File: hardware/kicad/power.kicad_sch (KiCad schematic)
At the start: 61 parts, among them J1 USB_C_Receptacle_USB2.0_16P, J2 BATT (1S LiPo), U1 BQ24073RGT, U2 TPS63802DLA, U3 TPS61023DRL, U4 TPS22965DSG, U5 USBLC6-2SC6, U6 TPS63900DSK, U7 MCP1700T-3002E/TT

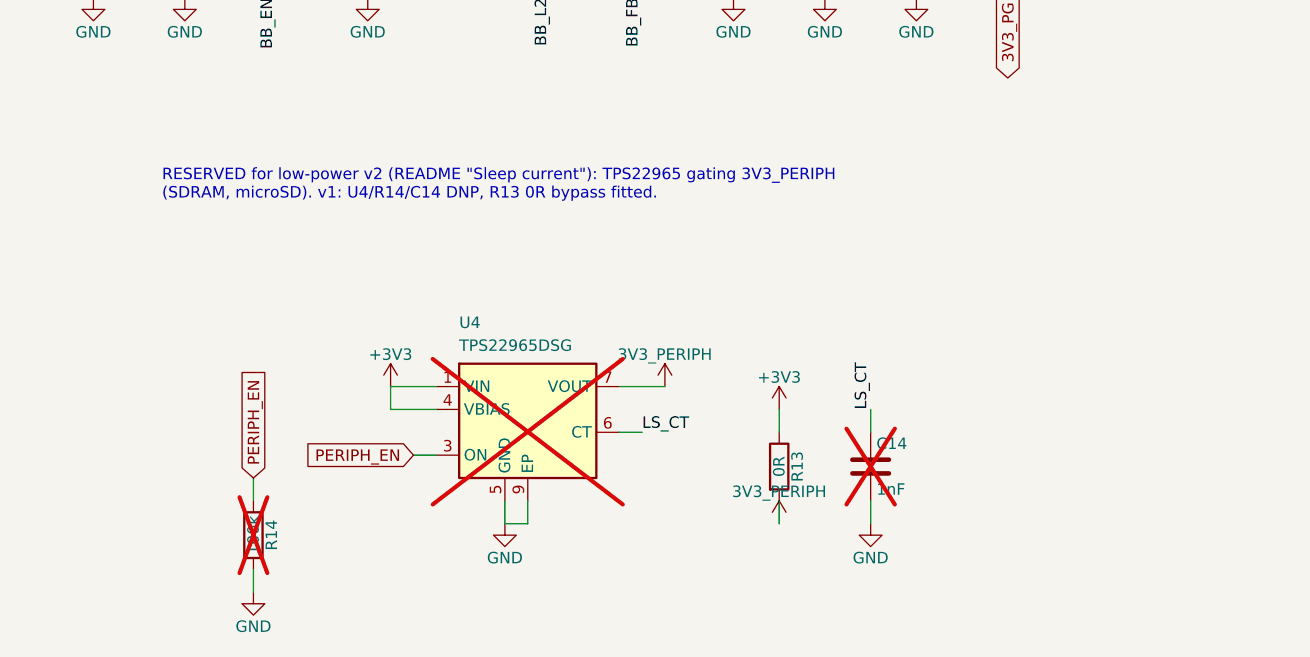
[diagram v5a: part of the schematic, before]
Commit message: Fit the TPS22965 peripheral load switch on v1
Without it SDRAM/QSPI/microSD stay powered in STANDBY (~2-20 mA idle floor,
~70 mAh/day); with it idle drops to ~0.5-2 mAh/day.

- U4 TPS22965 populated; R13 0R bypass -> DNP (fallback).
- R14 100k pull-down on PERIPH_EN (PD7) fitted: rail off at reset and
  automatically in STANDBY (GPIO hi-Z).
- C14 CT 1 nF, 25 V X7R (CT pin reaches 12 V): ~1.3 ms rise at 3.3 V
  (datasheet Table 1) -> ~50 mA inrush into ~21 uF of downstream decoupling.
- README/TODO: decision, firmware sequencing rules (enable before
  FMC/QSPI/SDIO init; pins to analog/low before disabling; re-init SDRAM and
  re-mount SD on wake), TPS63900 remains the only v2 reservation.

ERC 0 violations; check_schematic.py OK.

Co-Authored-By: Claude Opus 5.5 <noreply@anthropic.com>
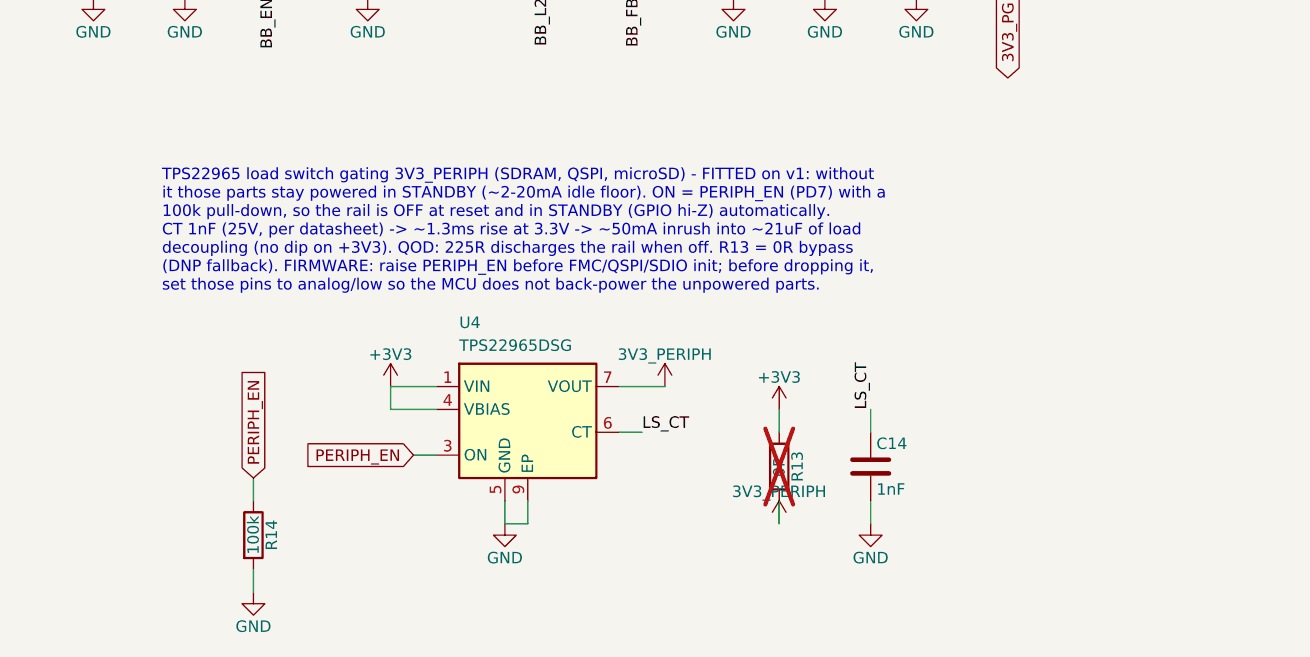
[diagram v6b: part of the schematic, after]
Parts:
- C14: Voltage (none) -> 25V X7R (CT pin can reach 12V); now fitted
- R13: now not fitted
- R14, U4: now fitted
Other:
- note added: "TPS22965 load switch gating 3V3_PERIPH (SDRAM, QSPI, microSD) - FITTED on v1: without it those parts stay powered in STANDBY (~2-20mA idle floor). ON = PERIPH_EN (PD7) with a 100k pull-down, so the rail is OFF at reset and in STANDBY (GPIO hi-Z) automatically. CT 1nF (25V, per datasheet) -> ~1.3ms rise at 3.3V -> ~50mA inrush into ~21uF of load decoupling (no dip on +3V3). QOD: 225R discharges th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"
- note removed: "RESERVED for low-power v2 (README "Sleep current"): TPS22965 gating 3V3_PERIPH (SDRAM, microSD). v1: U4/R14/C14 DNP, R13 0R bypass fitted."
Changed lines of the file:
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@@
 		)
 	)
-	(text "RESERVED for low-power v2 (README \"Sleep current\"): TPS22965 gating 3V3_PERIPH\n(SDRAM, microSD). v1: U4/R14/C14 DNP, R13 0R bypass fitted."
+	(text "TPS22965 load switch gating 3V3_PERIPH (SDRAM, QSPI, microSD) - FITTED on v1: without\nit those parts stay powered in STANDBY (~2-20mA idle floor). ON = PERIPH_EN (PD7) with a\n100k pull-down, so the rail is OFF at reset and in STANDBY (GPIO hi-Z) automatically.\nCT 1nF (25V, per datasheet) -> ~1.3ms rise at 3.3V -> ~50mA inrush into ~21uF of load\ndecoupling (no dip on +3V3). QOD: 225R discharges the rail when off. R13 = 0R bypass\n(DNP fallback). FIRMWARE: raise PERIPH_EN before FMC/QSPI/SDIO init; before dropping it,\nset those pins to analog/low so the MCU does not back-power the unpowered parts."
 		(exclude_from_sim no)
 		(at 137.16 236.22 0)
@@
 		(in_bom yes)
 		(on_board yes)
-		(dnp yes)
+		(dnp no)
 		(property "Reference" "U4"
 			(at 170.18 254 0)
@@
 		(in_bom yes)
 		(on_board yes)
-		(dnp no)
+		(dnp yes)
 		(property "Reference" "R13"
 			(at 207.772 269.24 90)
@@
 		(in_bom yes)
 		(on_board yes)
-		(dnp yes)
+		(dnp no)
 		(property "Reference" "R14"
 			(at 149.352 276.86 90)
@@
 		(in_bom yes)
 		(on_board yes)
-		(dnp yes)
+		(dnp no)
 		(property "Reference" "C14"
 			(at 216.535 266.7 0)
@@
 			(at 215.9 269.24 0)
 			(hide yes)
+			(effects
+				(font
+					(size 1.27 1.27)
+				)
+			)
+		)
+		(property "Voltage" "25V X7R (CT pin can reach 12V)"
+			(at 215.9 269.24 0)
+			(hide yes)

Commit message: Apply enclosure decisions: bottom-edge power button, electrode boards, leaded NTC
Decisions (2026-09-23): keep the HAT's 2x20 header for v1; move the power
button to the bottom edge; put the side-wall electrodes on two small
boards; keep the front-face knob; put RT1 on leads to the cell.

Schematic (via the generator scripts, check_schematic.py passes):
- SW302: Alps SKRTLAE010 side-actuated switch on the PCB's bottom edge.
- E301-E304 test pads -> J302/J303 JST-SH 3-pin (touch / GND / touch),
  cabled to the electrode boards.
- RT1: leaded Murata NXFT15XH103FA2B (same 10k/B3380 curve) on solder
  pads, head taped to the pouch.

Enclosure: flexure tab in the bottom wall over the switch; two identical
74 x 10 mm electrode boards in printed channels on the side walls; PCB
and battery 2.5 mm in from the walls to make room; new checks for the
button travel and electrode coverage (21 pass, no interferences);
electrode_board.json export and a bottom-edge render.

Co-Authored-By: Claude Opus 5.5 <noreply@anthropic.com>
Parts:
- RT1: footprint Resistor_SMD:R_0402_1005Metric -> Connector_Wire:SolderWire-0.1sqmm_1x02_P3.6mm_D0.4mm_OD1mm; MPN NCP15XH103F03RC (10k, B=3380; TS thresholds assume 103AT, B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 -> NXFT15XH103FA2B (Murata leaded film NTC: same 10k/B=3380 cu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
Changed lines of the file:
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@@
 			)
 		)
-		(property "Footprint" "Resistor_SMD:R_0402_1005Metric"
+		(property "Footprint" "Connector_Wire:SolderWire-0.1sqmm_1x02_P3.6mm_D0.4mm_OD1mm"
 			(at 172.72 111.76 0)
 			(hide yes)
@@
 			)
 		)
-		(property "MPN" "NCP15XH103F03RC (10k, B=3380; TS thresholds assume 103AT, B=3435) - place touching the cell"
+		(property "MPN" "NXFT15XH103FA2B (Murata leaded film NTC: same 10k/B=3380 curve as NCP15XH103; TS thresholds assume 103AT, B=3435) - leads soldered here, head taped to the cell (it sits beside the PCB)"
 			(at 172.72 111.76 0)
 			(hide yes)

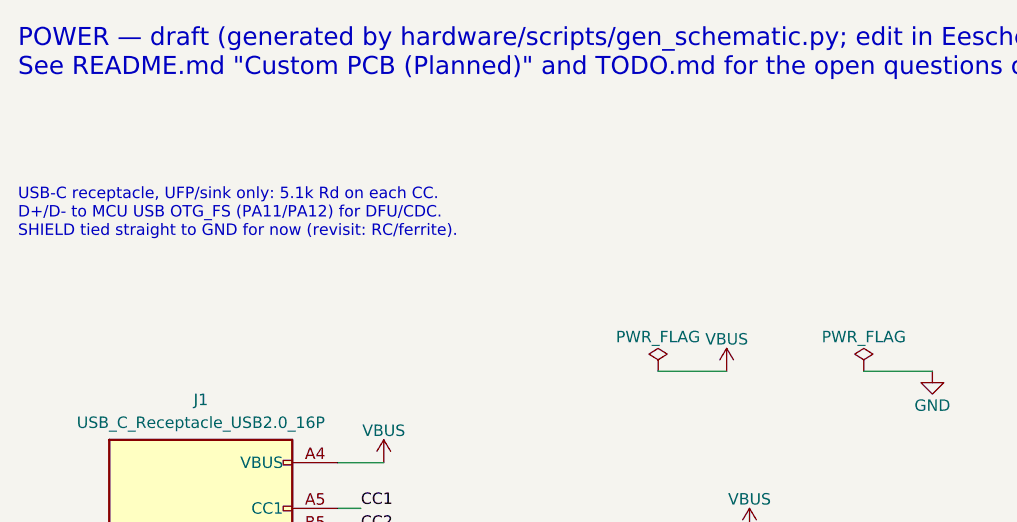
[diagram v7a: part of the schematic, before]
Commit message: Electrode board project, open hardware TODOs, main PCB bootstrap
- hardware/electrode/: side-wall electrode board (one design, two fitted),
  generated by gen_electrode.py (schematic, pad footprint) and
  gen_electrode_pcb.py (board, via KiCad's pcbnew Python) from the
  enclosure's params.py. ERC/DRC/parity clean.
- Datasheet values replace most enclosure placeholders. The encoder is now
  PEC11R-4220F-S0024 (20 mm shaft): the M7 bushing left the 15 mm shaft
  too short for the knob. Knob redesigned around the bushing.
- Schematic: TPD4E05U06 ESD on the electrode lines, HRDY 100k pull-down,
  crystals chosen (NX3225GD 8 MHz / NX3215SA 32.768 kHz) with recomputed
  load caps, all inductors DFE201612E, M2 mounting holes.
- Decisions recorded: USB shield to GND, UVLO restart analysis, soft power
  = STANDBY + WKUP, no fuel gauge on v1, TPS63900 footprint verified.
- Encoder footprint: silkscreen no longer crosses its own lug pads.
- hardware/kicad/stm32-epaper.kicad_pcb: 4-layer board bootstrapped by
  gen_main_pcb.py with the enclosure outline, all footprints and nets, and
  the enclosure-fixed parts placed.

Co-Authored-By: Claude Opus 5.5 <noreply@anthropic.com>
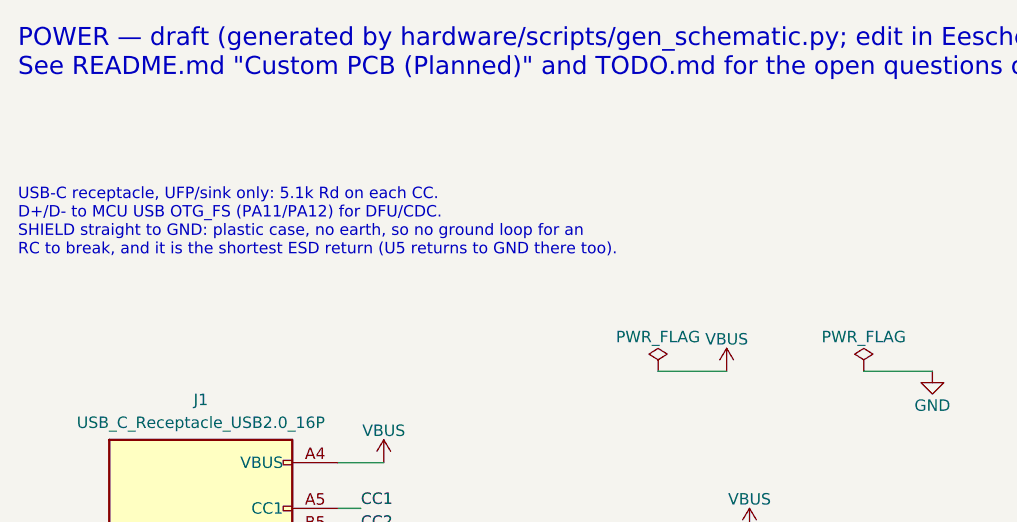
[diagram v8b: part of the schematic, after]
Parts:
- L1: MPN DFE201612E-R47M (TI Table 10-2: 5.5A Isat; verify land patt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 -> DFE201612E-R47M=P2 (Isat 5.5A, 26mR; Murata land = this foo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
- L2: MPN DFE201610P-1R0M (verify Isat vs 3.7A valley limit) -> DFE201612E-1R0M=P2 (Isat 4.0A >= TPS61023 3.7A valley limit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
- L3: MPN 2.2uH per TPS63900 datasheet; pick the part at v2 -> DFE201612E-2R2M=P2 (TPS63900 datasheet Table 8-2; Isat 2.4A)
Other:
- note added: "USB-C receptacle, UFP/sink only: 5.1k Rd on each CC. D+/D- to MCU USB OTG_FS (PA11/PA12) for DFU/CDC. SHIELD straight to GND: plastic case, no earth, so no ground loop for an RC to break, and it is the shortest ESD return (U5 returns to GND there too)."
- note removed: "USB-C receptacle, UFP/sink only: 5.1k Rd on each CC. D+/D- to MCU USB OTG_FS (PA11/PA12) for DFU/CDC. SHIELD tied straight to GND for now (revisit: RC/ferrite)."
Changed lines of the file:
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@@
 		)
 	)
-	(text "USB-C receptacle, UFP/sink only: 5.1k Rd on each CC.\nD+/D- to MCU USB OTG_FS (PA11/PA12) for DFU/CDC.\nSHIELD tied straight to GND for now (revisit: RC/ferrite)."
+	(text "USB-C receptacle, UFP/sink only: 5.1k Rd on each CC.\nD+/D- to MCU USB OTG_FS (PA11/PA12) for DFU/CDC.\nSHIELD straight to GND: plastic case, no earth, so no ground loop for an\nRC to break, and it is the shortest ESD return (U5 returns to GND there too)."
 		(exclude_from_sim no)
 		(at 20.32 30.48 0)
@@
 			)
 		)
-		(property "MPN" "DFE201612E-R47M (TI Table 10-2: 5.5A Isat; verify land pattern)"
+		(property "MPN" "DFE201612E-R47M=P2 (Isat 5.5A, 26mR; Murata land = this footprint)"
 			(at 180.34 210.82 0)
 			(hide yes)
@@
 			)
 		)
-		(property "MPN" "DFE201610P-1R0M (verify Isat vs 3.7A valley limit)"
+		(property "MPN" "DFE201612E-1R0M=P2 (Isat 4.0A >= TPS61023 3.7A valley limit, 48mR)"
 			(at 284.48 210.82 0)
 			(hide yes)
@@
 			)
 		)
-		(property "MPN" "2.2uH per TPS63900 datasheet; pick the part at v2"
+		(property "MPN" "DFE201612E-2R2M=P2 (TPS63900 datasheet Table 8-2; Isat 2.4A)"
 			(at 363.22 104.14 0)
 			(hide yes)
